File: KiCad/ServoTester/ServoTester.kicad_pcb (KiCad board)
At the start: 2 copper layers, 14 parts, among them J1 WiiNunchuckConnector, J2 Conn_01x02_Female, M1 Motor_Servo_JR, M2 Motor_Servo_JR, M3 Motor_Servo_JR, M4 Motor_Servo_JR, U1 Teensy2.0, U2 HD44780

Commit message: think board is ready for prototyping
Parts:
- added C1: CP1, Capacitor_THT:CP_Radial_D8.0mm_P5.00mm, F.Cu at (127.0, 123.2)
- added R2: R_US, Resistor_THT:R_Axial_DIN0207_L6.3mm_D2.5mm_P10.16mm_Horizontal, F.Cu at (102.9, 141.6)
- added REF**: OSHW-Logo_11.4x12mm_SilkScreen, Symbol:OSHW-Logo_11.4x12mm_SilkScreen, F.Cu at (138.4, 144.1)
- added SW1: SW_Push_Open, Button_Switch_THT:SW_PUSH_6mm_H5mm, F.Cu at (104.8, 130.8)
- RV1: footprint Connector_Wire:SolderWirePad_1x03_P3.175mm_Drill1mm -> ServoTester:Potentiometer
- moved J1 123.4 mm to (109.2, 154.9), turned to 180 degrees
- moved RV1 79.5 mm to (108.0, 117.5), turned to 270 degrees
- moved U1 57.6 mm to (85.1, 137.2)
- moved J2 55.7 mm to (65.4, 117.5), turned to 270 degrees
- moved M1 44.9 mm to (135.9, 134.6)
- moved JP1 44.9 mm to (135.9, 121.9)
- moved M2 44.9 mm to (142.2, 134.6)
- moved M3 44.9 mm to (148.6, 134.6)
- moved M4 44.9 mm to (154.9, 134.6)
- moved JP2 44.9 mm to (142.2, 121.9)
- moved JP3 44.9 mm to (148.6, 121.9)
- moved JP4 44.9 mm to (154.9, 121.9)
- moved R1 30.0 mm to (82.5, 56.5), turned to 0 degrees
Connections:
- U2 pad 4: Net-(U1-Pad23) -> Net-(U1-Pad24)
- U2 pad 6: Net-(U1-Pad24) -> Net-(U1-Pad23)
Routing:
- net VCC: track 0.00 -> 209.6 mm, vias 0 -> 1
- net Net-(U1-Pad28): track 0.00 -> 107.2 mm
- net Net-(U1-Pad27): track 0.00 -> 103.6 mm
- net Net-(U1-Pad26): track 0.00 -> 100.9 mm
- net Net-(U1-Pad25): track 0.00 -> 96.4 mm
- net Net-(J2-Pad1): track 0.00 -> 93.0 mm
- net Net-(U1-Pad24): track 0.00 -> 89.2 mm
- net Net-(U1-Pad23): track 0.00 -> 87.6 mm
- net Net-(M4-Pad1): track 0.00 -> 80.9 mm
- net Net-(RV1-Pad2): track 0.00 -> 80.2 mm, vias 0 -> 3
- net Net-(M3-Pad1): track 0.00 -> 74.3 mm
- net Net-(M2-Pad1): track 0.00 -> 54.3 mm
- net Net-(M1-Pad1): track 0.00 -> 46.9 mm
- net Net-(R2-Pad2): track 0.00 -> 31.8 mm
- net Net-(J1-Pad3): track 0.00 -> 27.5 mm, vias 0 -> 1
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- added copper zone on B.Cu, net GND
- added copper zone on F.Cu, net GND
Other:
- board outline added: 101.6 x 107.3 mm
- net class Power added: clearance 0.2, trace_width 0.5, via_dia 1, via_drill 0.5
- board text added: "https://github.com/m000z0rz/ServoTester"

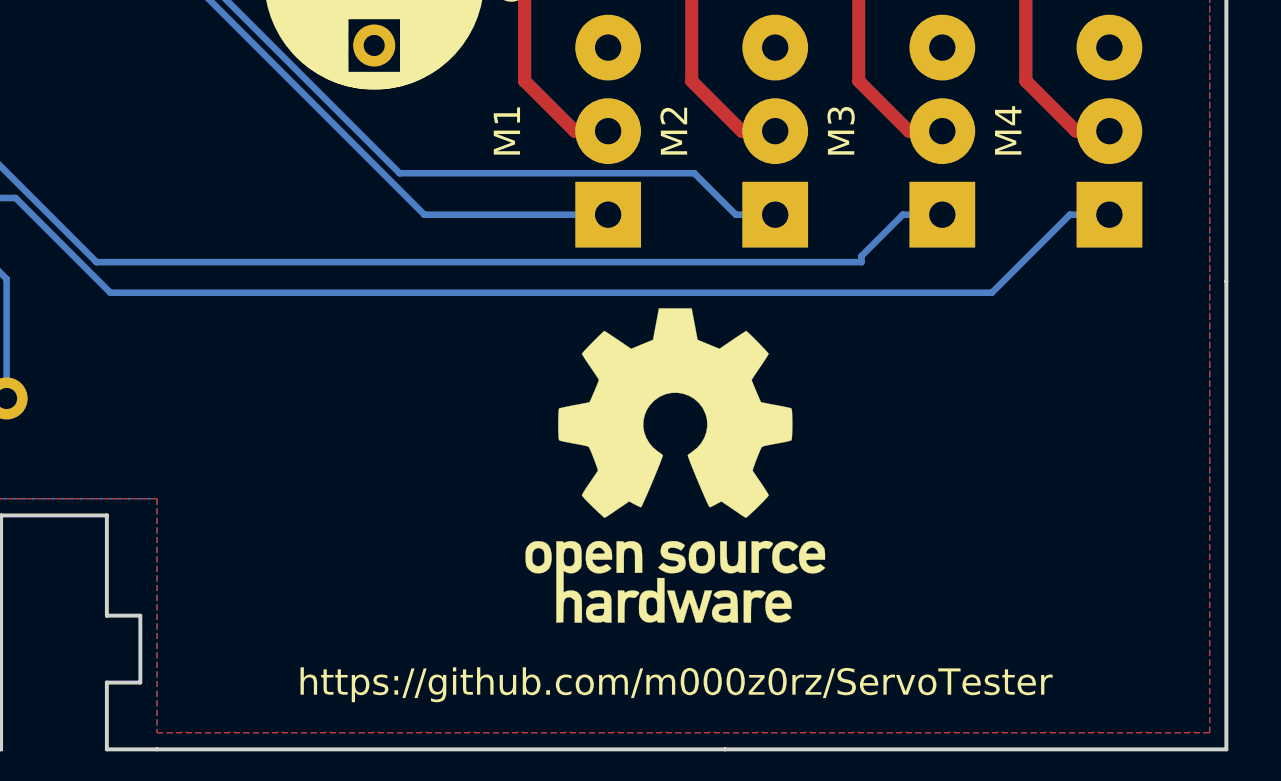
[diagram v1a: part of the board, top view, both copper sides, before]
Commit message: board labels, and software: don't require stick movement for save, notify saved on lcd, fix deg<->pms conversion, ...
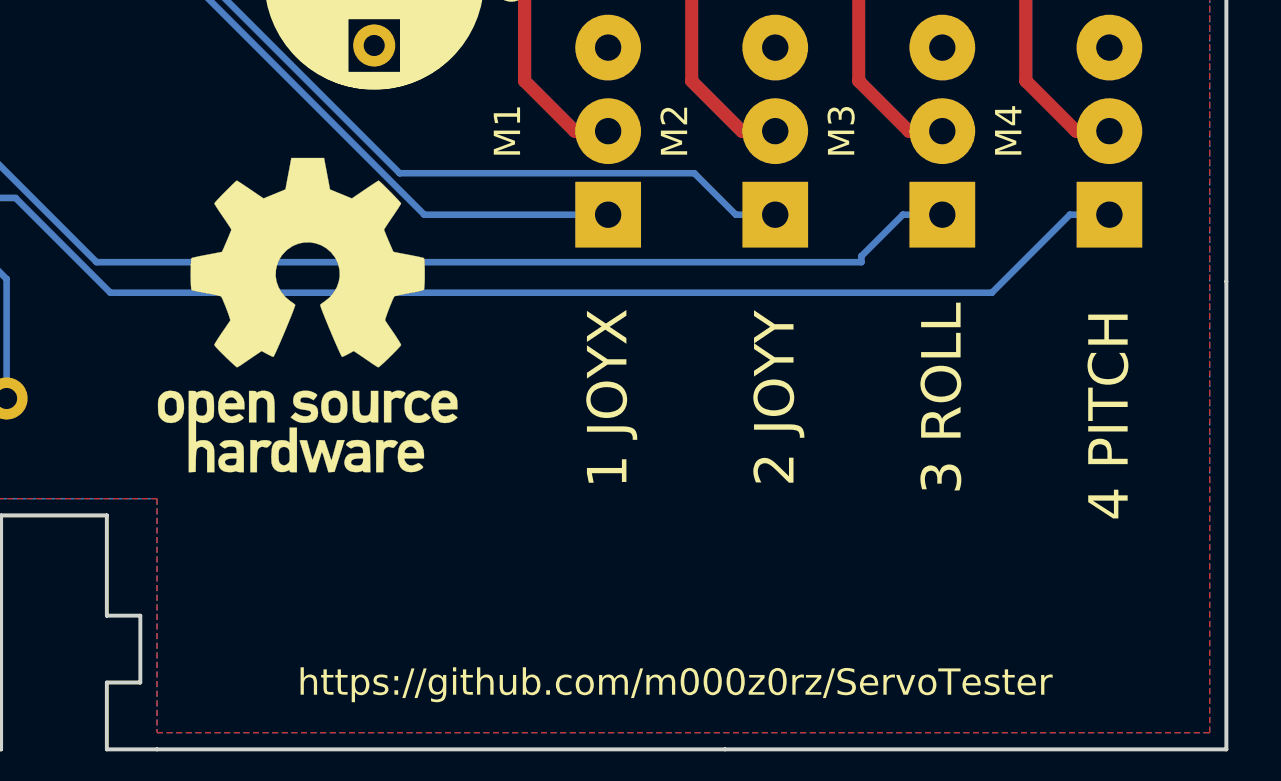
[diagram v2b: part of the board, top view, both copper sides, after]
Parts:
- moved REF** 15.1 mm to (124.5, 138.4)
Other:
- board text added: "1 JOYX"
- board text added: "2 JOYY"
- board text added: "3 ROLL"
- board text added: "4 PITCH"
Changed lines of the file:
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@@
   (general
     (thickness 1.6)
-    (drawings 29)
+    (drawings 33)
     (tracks 134)
     (zones 0)
@@
   )
   (module Symbol:OSHW-Logo_11.4x12mm_SilkScreen (layer F.Cu)
-    (at 138.43 144.145)
+    (at 124.46 138.43)
     (descr "Open Source Hardware Logo")
     (tags "Logo OSHW")
@@
       (xy -3.904571 2.880953) (xy -3.780091 2.90956)) (layer F.SilkS) (width 0.01))
   )
+  (gr_text "2 JOYY" (at 142.24 141.605 90) (layer F.SilkS)
+    (effects (font (size 1.5 1.5) (thickness 0.3)))
+  )
+  (gr_text "1 JOYX" (at 135.89 141.605 90) (layer F.SilkS)
+    (effects (font (size 1.5 1.5) (thickness 0.3)))
+  )
+  (gr_text "4 PITCH" (at 154.94 142.24 90) (layer F.SilkS)
+    (effects (font (size 1.5 1.5) (thickness 0.3)))
+  )
+  (gr_text "3 ROLL" (at 148.59 141.605 90) (layer F.SilkS)
+    (effects (font (size 1.5 1.5) (thickness 0.3)))
+  )
   (gr_text https://github.com/m000z0rz/ServoTester (at 138.43 152.4) (layer F.SilkS)

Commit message: fixing board
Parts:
- J2: footprint Connector:Banana_Jack_2Pin -> ServoTester:BananaJack_2
- JP1, JP2, JP3, JP4, M1, M2, M3, M4: footprint Connector_Wire:SolderWirePad_1x03_P3.175mm_Drill1mm -> Connector_PinHeader_2.54mm:PinHeader_1x03_P2.54mm_Vertical
- moved J2 0.64 mm to (66.0, 117.5), turned to 0 degrees
- turned JP1 to 180 degrees
- turned JP2 to 180 degrees
- turned JP3 to 180 degrees
- turned JP4 to 180 degrees
- turned M1 to 180 degrees
- turned M2 to 180 degrees
- turned M3 to 180 degrees
- turned M4 to 180 degrees
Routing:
- net Net-(J2-Pad1): track 93.0 -> 93.5 mm
- net Net-(JP4-Pad2): track 16.8 -> 16.3 mm
- net Net-(JP3-Pad2): track 16.8 -> 16.3 mm
- net Net-(JP1-Pad2): track 16.8 -> 16.3 mm
- net Net-(JP2-Pad2): track 16.8 -> 16.3 mm
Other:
- outline, holes or cut-outs redrawn
